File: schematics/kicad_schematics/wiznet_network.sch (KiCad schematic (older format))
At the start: 50 parts

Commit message: Cleaned up Schematic File and modified SD card module, bearboard schematic
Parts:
- gave numbers to parts that had none: 50

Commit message: Updated USB connector to change the sheild pin to power input Updated the schematic to fix some schematic electrical issues
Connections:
- net labels removed: GNDPWR
- no-connect marks 15 -> 17

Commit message: back annotated footprints into eeschem schematic
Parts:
- C14, C15, C16, C17, C18, C19, C20, C21, C22, C24, C25, C26, C27, C28, C29, C30, C31, C33, R39, R40, R41, R42, R43, R44, R45, R46, R47, R48, R49, R50, R51, R52, R53: footprint (none) -> SM0805
- C23, C32, C34: footprint (none) -> SM1210L
- D10, D11, D12, D8, D9: footprint (none) -> LED-0805
- U6: footprint (none) -> -LQFP100
- U7: footprint (none) -> MagJack
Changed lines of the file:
@@
-EESchema Schematic File Version 2  date Wed 10 Mar 2010 08:20:30 PM EST
+EESchema Schematic File Version 2  date Fri 12 Mar 2010 11:31:07 AM EST
 LIBS:power
 LIBS:device
@@
 F 0 "R43" H 9450 9200 50  0000 C CNN
 F 1 "1M" V 9550 9200 50  0000 C CNN
+F 2 "SM0805" H 9550 9200 60  0001 C CNN
 	1    9550 9200
 	-1   0    0    1
@@
 F 0 "C15" V 8700 9750 50  0000 L CNN
 F 1 "18pF" V 8700 9450 50  0000 L CNN
+F 2 "SM0805" H 8650 9600 60  0001 C CNN
 	1    8650 9600
 	0    -1   -1   0
@@
 F 0 "C14" V 8700 8950 50  0000 L CNN
 F 1 "18pF" V 8700 8650 50  0000 L CNN
+F 2 "SM0805" H 8650 8800 60  0001 C CNN
 	1    8650 8800
 	0    -1   -1   0
@@
 F 0 "R44" H 9500 5200 50  0000 C CNN
 F 1 "49.9" V 9600 5200 50  0000 C CNN
+F 2 "SM0805" H 9600 5200 60  0001 C CNN
 	1    9600 5200
 	-1   0    0    1
@@
 F 0 "R41" H 9200 5200 50  0000 C CNN
 F 1 "49.9" V 9300 5200 50  0000 C CNN
+F 2 "SM0805" H 9300 5200 60  0001 C CNN
 	1    9300 5200
 	-1   0    0    1
@@
 F 0 "C16" H 10200 6800 50  0000 L CNN
 F 1 "0.1uF" H 9900 6600 50  0000 L CNN
+F 2 "SM0805" H 10150 6700 60  0001 C CNN
 	1    10150 6700
 	1    0    0    -1
@@
 F 0 "R47" H 10600 5200 50  0000 C CNN
 F 1 "200" V 10700 5200 50  0000 C CNN
+F 2 "SM0805" H 10700 5200 60  0001 C CNN
 	1    10700 5200
 	-1   0    0    1
@@
 F 0 "R46" H 10300 5200 50  0000 C CNN
 F 1 "200" V 10400 5200 50  0000 C CNN
+F 2 "SM0805" H 10400 5200 60  0001 C CNN
 	1    10400 5200
 	-1   0    0    1
@@
 F 0 "R42" H 9200 7000 50  0000 C CNN
 F 1 "49.9" V 9300 7000 50  0000 C CNN
+F 2 "SM0805" H 9300 7000 60  0001 C CNN
 	1    9300 7000
 	-1   0    0    1
@@
 F 0 "R45" H 9500 7000 50  0000 C CNN
 F 1 "49.9" V 9600 7000 50  0000 C CNN
+F 2 "SM0805" H 9600 7000 60  0001 C CNN
 	1    9600 7000
 	-1   0    0    1
@@
 F 0 "U7" H 11450 7350 60  0000 C CNN
 F 1 "RD1-125BAG1A" H 11750 5550 60  0000 C CNN
+F 2 "MagJack" H 11400 6400 60  0001 C CNN
 	1    11400 6400
 	1    0    0    -1
@@
 F 0 "R52" V 10930 3950 50  0000 C CNN
 F 1 "330" V 10850 3950 50  0000 C CNN
+F 2 "SM0805" H 10850 3950 60  0001 C CNN
 	1    10850 3950
 	0    -1   -1   0
@@
 F 0 "D12" H 10300 4050 50  0000 C CNN
 F 1 "LED" H 10300 3850 50  0000 C CNN
+F 2 "LED-0805" H 10300 3950 60  0001 C CNN
 	1    10300 3950
 	-1   0    0    1
@@
 F 0 "D11" H 10300 3750 50  0000 C CNN
 F 1 "LED" H 10300 3550 50  0000 C CNN
+F 2 "LED-0805" H 10300 3650 60  0001 C CNN
 	1    10300 3650
 	-1   0    0    1
@@
 F 0 "R51" V 10930 3650 50  0000 C CNN
 F 1 "330" V 10850 3650 50  0000 C CNN
+F 2 "SM0805" H 10850 3650 60  0001 C CNN
 	1    10850 3650
 	0    -1   -1   0
@@
 F 0 "R50" V 10930 3350 50  0000 C CNN
 F 1 "330" V 10850 3350 50  0000 C CNN
+F 2 "SM0805" H 10850 3350 60  0001 C CNN
 	1    10850 3350
 	0    -1   -1   0
@@
 F 0 "D10" H 10300 3450 50  0000 C CNN
 F 1 "LED" H 10300 3250 50  0000 C CNN
+F 2 "LED-0805" H 10300 3350 60  0001 C CNN
 	1    10300 3350
 	-1   0    0    1
@@
 F 0 "D8" H 10300 2850 50  0000 C CNN
 F 1 "LED" H 10300 2650 50  0000 C CNN
+F 2 "LED-0805" H 10300 2750 60  0001 C CNN
 	1    10300 2750
 	-1   0    0    1
@@
 F 0 "R48" V 10930 2750 50  0000 C CNN
 F 1 "330" V 10850 2750 50  0000 C CNN
+F 2 "SM0805" H 10850 2750 60  0001 C CNN
 	1    10850 2750
 	0    -1   -1   0
@@
 F 0 "R49" V 10930 3050 50  0000 C CNN
 F 1 "330" V 10850 3050 50  0000 C CNN
+F 2 "SM0805" H 10850 3050 60  0001 C CNN
 	1    10850 3050
 	0    -1   -1   0
@@
 F 0 "D9" H 10300 3150 50  0000 C CNN
 F 1 "LED" H 10300 2950 50  0000 C CNN
+F 2 "LED-0805" H 10300 3050 60  0001 C CNN
 	1    10300 3050
 	-1   0    0    1
@@
 F 0 "R53" H 10850 1300 50  0000 C CNN
 F 1 "4.7K" V 10950 1500 50  0000 C CNN
+F 2 "SM0805" H 10950 1500 60  0001 C CNN
 	1    10950 1500
 	-1   0    0    1
@@
 F 0 "C20" H 13200 5400 50  0000 L CNN
 F 1 "10uf/16V" H 12750 5200 50  0000 L CNN
+F 2 "SM0805" H 13150 5300 60  0001 C CNN
 F 4 "Tant" H 13150 5300 60  0001 C CNN "TypeOfCap"
 	1    13150 5300
@@
 F 0 "C24" H 13500 5400 50  0000 L CNN
 F 1 "0.1uF" H 13500 5200 50  0000 L CNN
+F 2 "SM0805" H 13450 5300 60  0001 C CNN
 	1    13450 5300
 	1    0    0    -1
@@
 F 0 "C32" H 14450 5400 50  0000 L CNN
 F 1 "10uF/16V" H 14450 5200 50  0000 L CNN
+F 2 "SM1210L" H 14400 5300 60  0001 C CNN
 F 4 "Tant" H 14400 5300 60  0001 C CNN "TypeOfCap"
 	1    14400 5300
@@
 F 0 "C31" H 14450 3950 50  0000 L CNN
 F 1 "0.1uF" H 14450 3750 50  0000 L CNN
+F 2 "SM0805" H 14400 3850 60  0001 C CNN
 	1    14400 3850
 	1    0    0    -1
@@
 F 0 "C34" H 14750 3950 50  0000 L CNN
 F 1 "10uF/16V" H 14750 3750 50  0000 L CNN
+F 2 "SM1210L" H 14700 3850 60  0001 C CNN
 F 4 "Tant" H 14700 3850 60  0001 C CNN "TypeOfCap"
 	1    14700 3850
@@
 F 0 "C23" H 13500 3950 50  0000 L CNN
 F 1 "3.3uF_Tant" H 13500 3750 50  0000 L CNN
+F 2 "SM1210L" H 13450 3850 60  0001 C CNN
 F 4 "Tant" H 13450 3850 60  0001 C CNN "TypeOfCap"
 	1    13450 3850
@@
 F 0 "C19" H 13200 3950 50  0000 L CNN
 F 1 "10uF" H 13200 3750 50  0000 L CNN
+F 2 "SM0805" H 13150 3850 60  0001 C CNN
 	1    13150 3850
 	1    0    0    -1
@@
 F 0 "C18" H 13200 2900 50  0000 L CNN
 F 1 "0.1uF" H 13200 2700 50  0000 L CNN
+F 2 "SM0805" H 13150 2800 60  0001 C CNN
 	1    13150 2800
 	1    0    0    -1
@@
 F 0 "C22" H 13500 2900 50  0000 L CNN
 F 1 "0.1uF" H 13500 2700 50  0000 L CNN
+F 2 "SM0805" H 13450 2800 60  0001 C CNN
 	1    13450 2800
 	1    0    0    -1
@@
 F 0 "C26" H 13800 2900 50  0000 L CNN
 F 1 "0.1uF" H 13800 2700 50  0000 L CNN
+F 2 "SM0805" H 13750 2800 60  0001 C CNN
 	1    13750 2800
 	1    0    0    -1
@@
 F 0 "C28" H 14100 2900 50  0000 L CNN
 F 1 "0.1uF" H 14100 2700 50  0000 L CNN
+F 2 "SM0805" H 14050 2800 60  0001 C CNN
 	1    14050 2800
 	1    0    0    -1
@@
 F 0 "C30" H 14400 2900 50  0000 L CNN
 F 1 "0.1uF" H 14400 2700 50  0000 L CNN
+F 2 "SM0805" H 14350 2800 60  0001 C CNN
 	1    14350 2800
 	1    0    0    -1
@@
 F 0 "C33" H 14700 2900 50  0000 L CNN
 F 1 "0.1uF" H 14700 2700 50  0000 L CNN
+F 2 "SM0805" H 14650 2800 60  0001 C CNN
 	1    14650 2800
 	1    0    0    -1
@@
 F 0 "C29" H 14400 1850 50  0000 L CNN
 F 1 "0.1uF" H 14400 1650 50  0000 L CNN
+F 2 "SM0805" H 14350 1750 60  0001 C CNN
 	1    14350 1750
 	1    0    0    -1
@@
 F 0 "C27" H 14100 1850 50  0000 L CNN
 F 1 "0.1uF" H 14100 1650 50  0000 L CNN
+F 2 "SM0805" H 14050 1750 60  0001 C CNN
 	1    14050 1750
 	1    0    0    -1
@@
 F 0 "C25" H 13800 1850 50  0000 L CNN
 F 1 "0.1uF" H 13800 1650 50  0000 L CNN
+F 2 "SM0805" H 13750 1750 60  0001 C CNN
 	1    13750 1750
 	1    0    0    -1
@@
 F 0 "C21" H 13500 1850 50  0000 L CNN
 F 1 "0.1uF" H 13500 1650 50  0000 L CNN
+F 2 "SM0805" H 13450 1750 60  0001 C CNN
 	1    13450 1750
 	1    0    0    -1
@@
 F 0 "C17" H 13200 1850 50  0000 L CNN
 F 1 "0.1uF" H 13200 1650 50  0000 L CNN
+F 2 "SM0805" H 13150 1750 60  0001 C CNN
 	1    13150 1750
 	1    0    0    -1
@@
 F 0 "R40" V 6830 2350 50  0000 C CNN
 F 1 "300" V 6750 2350 50  0000 C CNN
+F 2 "SM0805" H 6750 2350 60  0001 C CNN
 	1    6750 2350
 	0    1    1    0
@@
 F 0 "R39" V 6230 2350 50  0000 C CNN
 F 1 "12K" V 6150 2350 50  0000 C CNN
+F 2 "SM0805" H 6150 2350 60  0001 C CNN
 	1    6150 2350
 	0    1    1    0
@@
 F 0 "U6" H 3100 6700 60  0000 C CNN
 F 1 "W5300" H 4150 4250 60  0000 C CNN
+F 2 "-LQFP100" H 4250 4300 60  0001 C CNN
 	1    4250 4300
 	1    0    0    -1

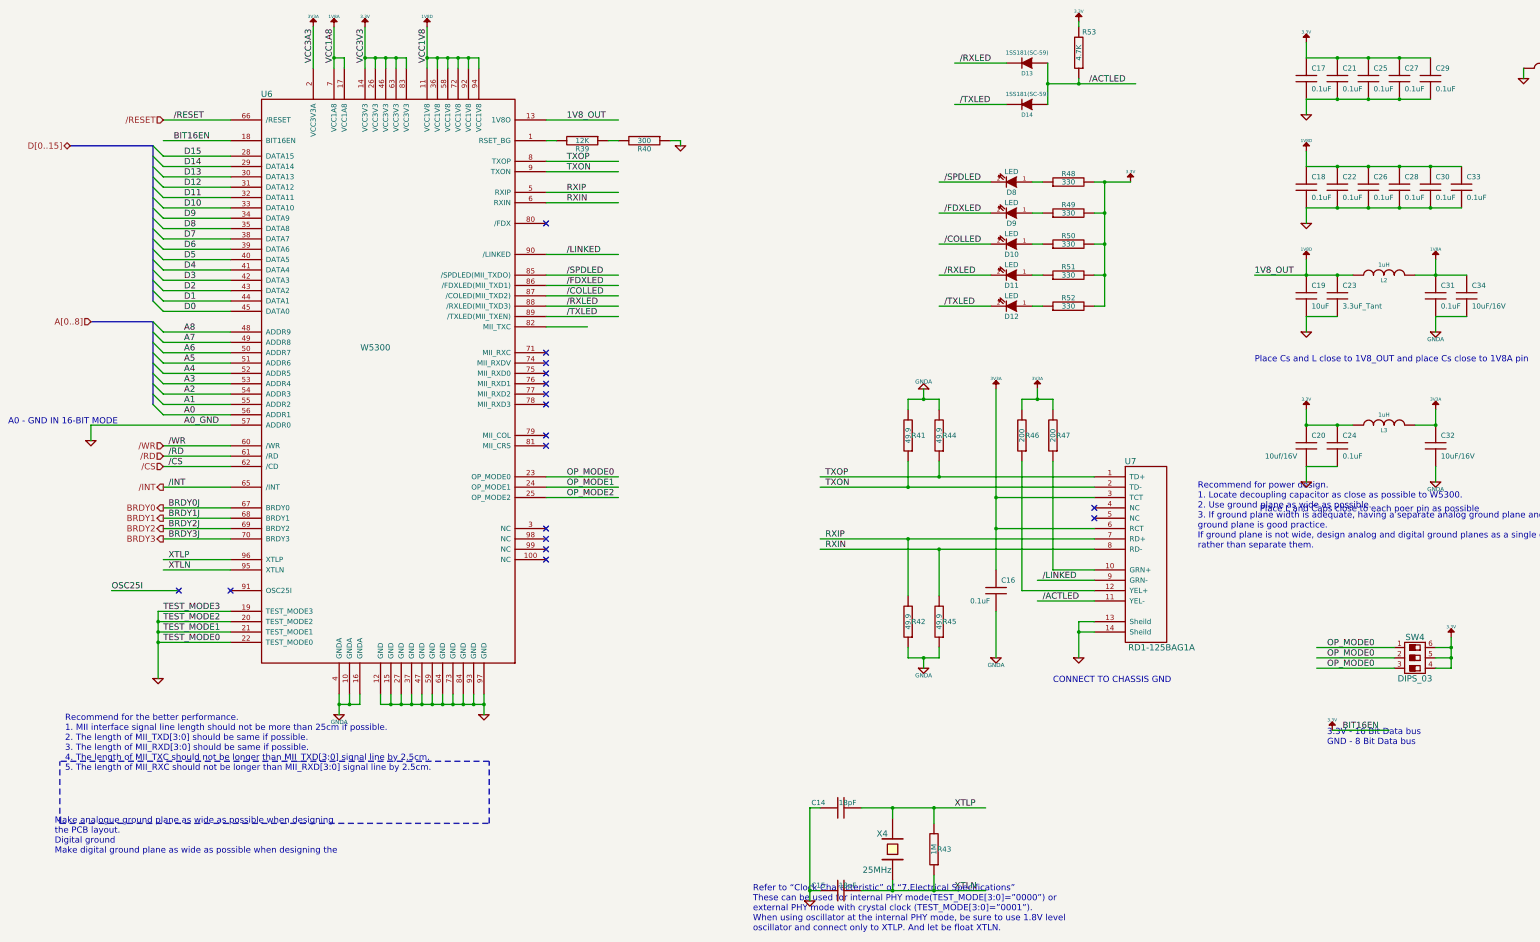
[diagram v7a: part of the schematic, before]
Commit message: added some more data sheets
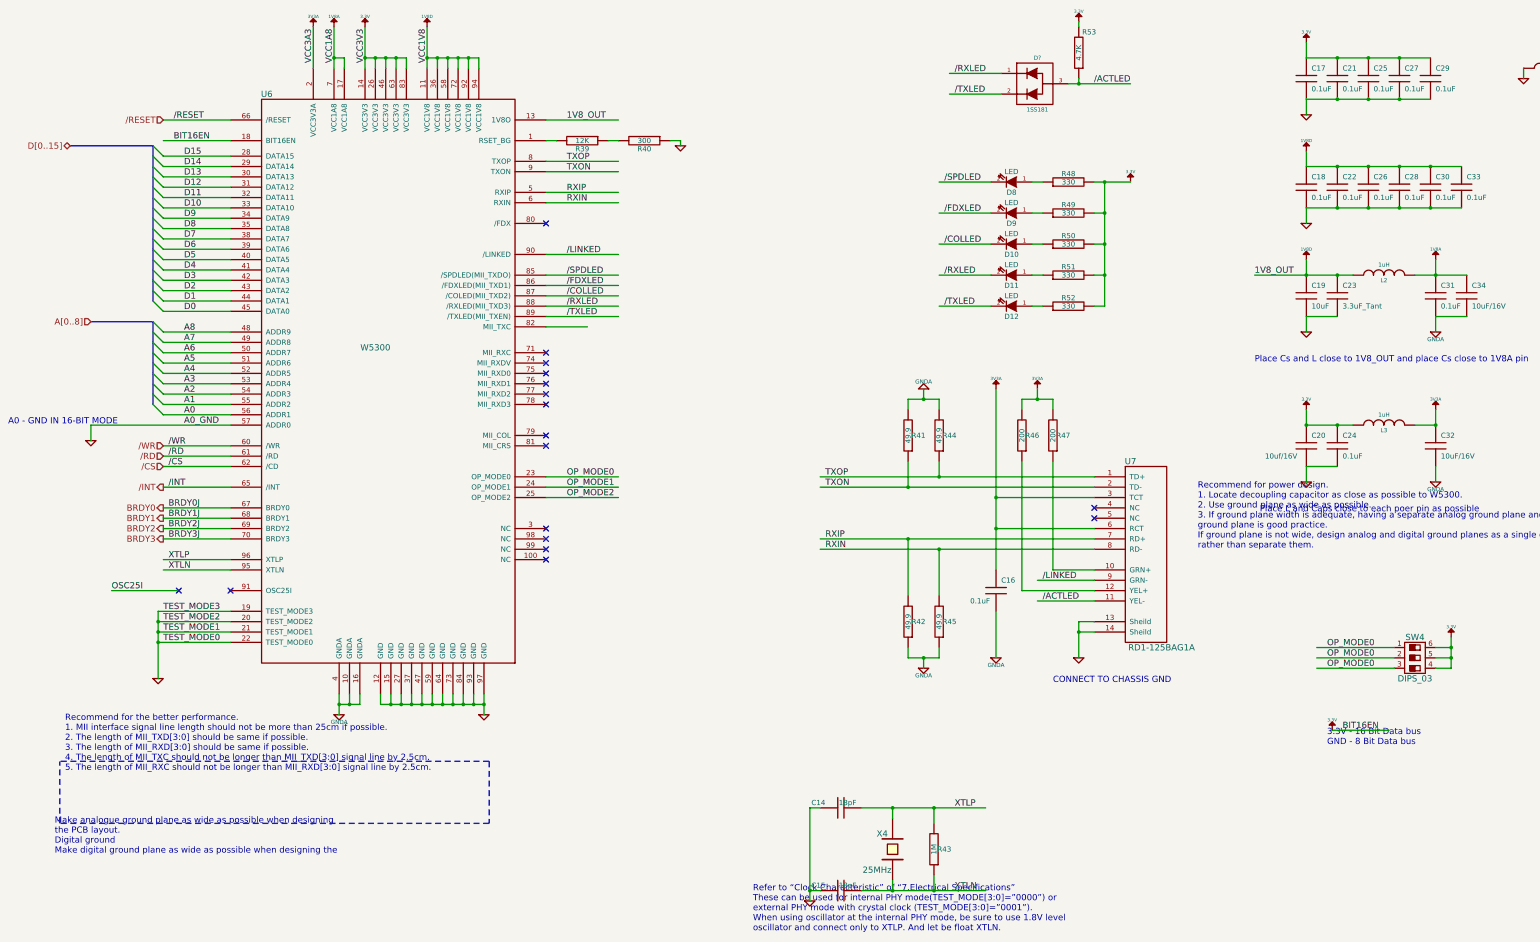
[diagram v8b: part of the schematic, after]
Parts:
- removed D13, D14: 1SS181(SC-59), symbol DIODE
- added D?: 1SS181, symbol 1SS181
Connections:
- wire segments 194 -> 193
